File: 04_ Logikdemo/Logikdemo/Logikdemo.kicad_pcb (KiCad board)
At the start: 2 copper layers, 83.5 x 44.7 mm, 29 parts, among them J1 Screw_Terminal_01x02, Q1 BC547, Q2 BC547, Q3 BC547, Q4 BC547, Q5 BC547, Q6 BC547, SW1 SW_Push, SW2 SW_Push, SW3 SW_Push, SW4 SW_Push, SW5 SW_Push

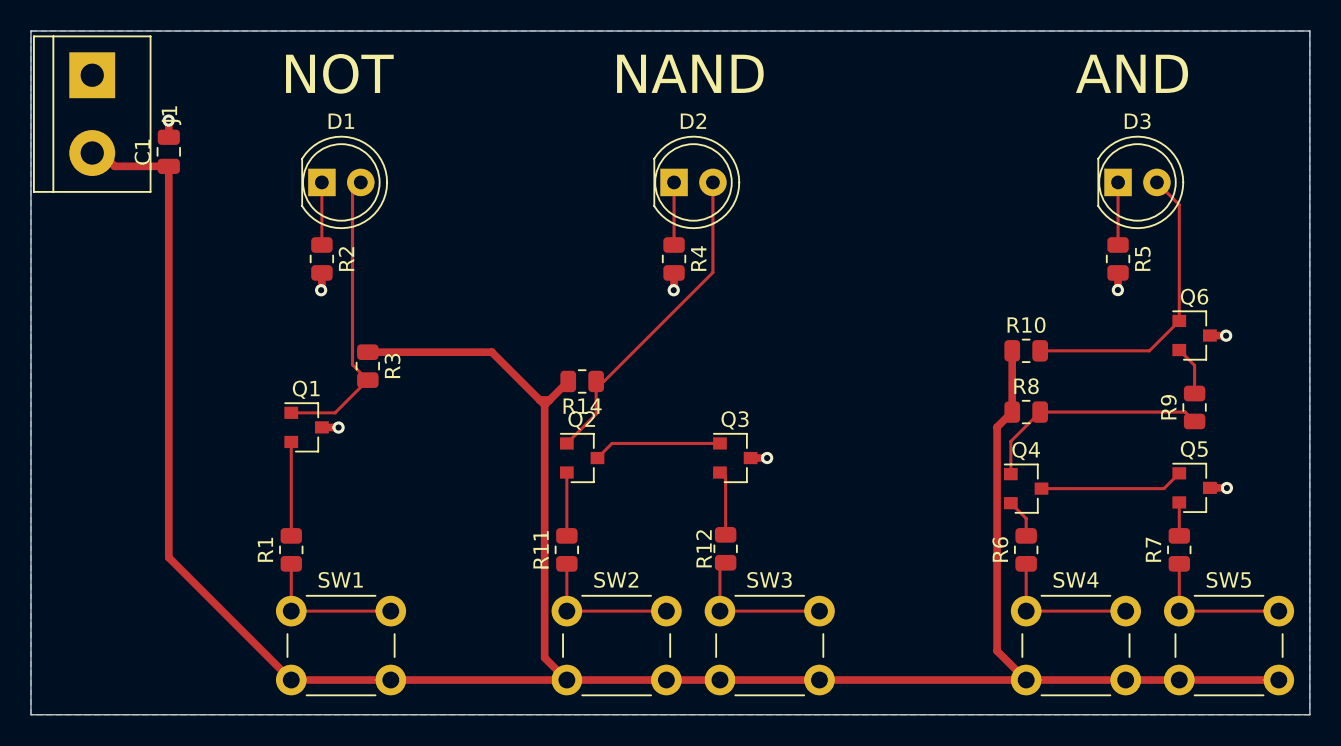
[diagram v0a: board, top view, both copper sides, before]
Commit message: relayouted 04
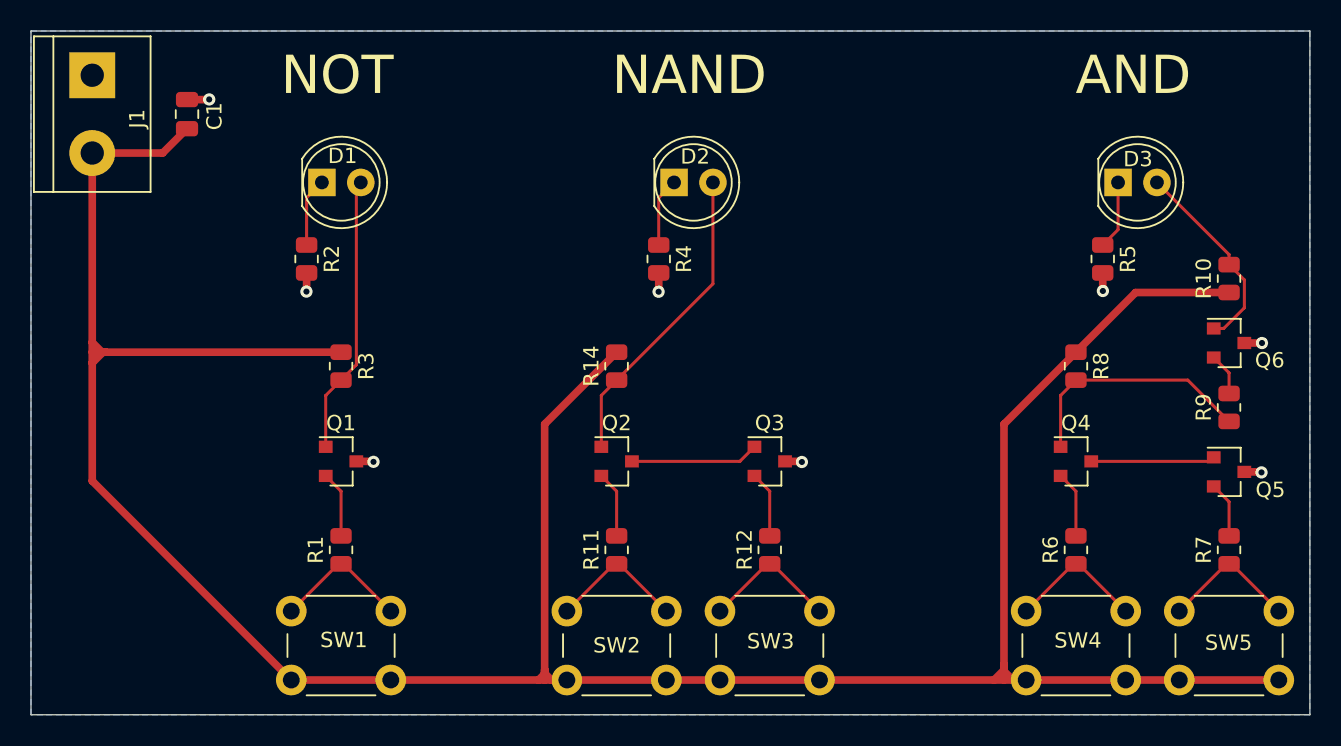
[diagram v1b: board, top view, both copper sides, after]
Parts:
- moved R10 14.1 mm to (143.2, 103.3), turned to 90 degrees
- moved R8 4.42 mm to (133.2, 109.0), turned to 270 degrees
- moved Q4 3.71 mm to (133.2, 115.2)
- moved R1 3.25 mm to (85.2, 121.0)
- moved R11 3.25 mm to (103.2, 121.0)
- moved R6 3.25 mm to (133.2, 121.0)
- moved R7 3.25 mm to (143.2, 121.0)
- moved Q1 3.16 mm to (85.2, 115.2)
- moved R12 2.88 mm to (113.2, 121.0)
- moved C1 2.73 mm to (75.2, 92.5)
- moved Q5 2.48 mm to (143.2, 115.9)
- moved R14 2.46 mm to (103.2, 109.0), turned to 90 degrees
- moved Q6 2.30 mm to (143.2, 107.5)
- moved Q2 2.26 mm to (103.2, 115.2)
- moved Q3 2.26 mm to (113.2, 115.2)
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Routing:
- net VCC: track 163.8 -> 192.3 mm
- net Q_3: track 19.5 -> 13.1 mm
- net Net-(Q1-Pad2): track 6.14 -> 4.33 mm
- net Net-(Q4-Pad2): track 2.55 -> 4.33 mm
- net Net-(Q5-Pad2): track 2.19 -> 3.65 mm
- net Net-(Q4-Pad3): track 9.41 -> 8.11 mm
- net Q_1: track 19.4 -> 18.2 mm
- net Q_2: track 21.3 -> 20.3 mm
- net GND: track 8.85 -> 9.62 mm
- net B_2: track 9.81 -> 9.06 mm
- net Net-(Q4-Pad1): track 15.2 -> 15.9 mm
- net B_3: track 9.59 -> 9.06 mm
- net A_3: track 9.59 -> 9.06 mm
- net A_2: track 9.59 -> 9.06 mm
- net A_1: track 9.59 -> 9.06 mm

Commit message: review
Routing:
- net VCC: track 192.3 -> 199.7 mm
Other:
- board text added: "GND"
- board text added: "VCC"
